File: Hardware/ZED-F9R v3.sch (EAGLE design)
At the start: 75 parts, among them J3 QWIIC_RIGHT_ANGLE, J4 QWIIC_RIGHT_ANGLE, U1 DUAL-OPTO_HCPL-073LSOIC-8, U2 U-BLOX_ZED_F9R, U3 UHS_INVERTER_SCHMITT_TRIGGERS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, U4 UHS_INVERTER_SCHMITT_TRIGGERS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, U5 3.3V

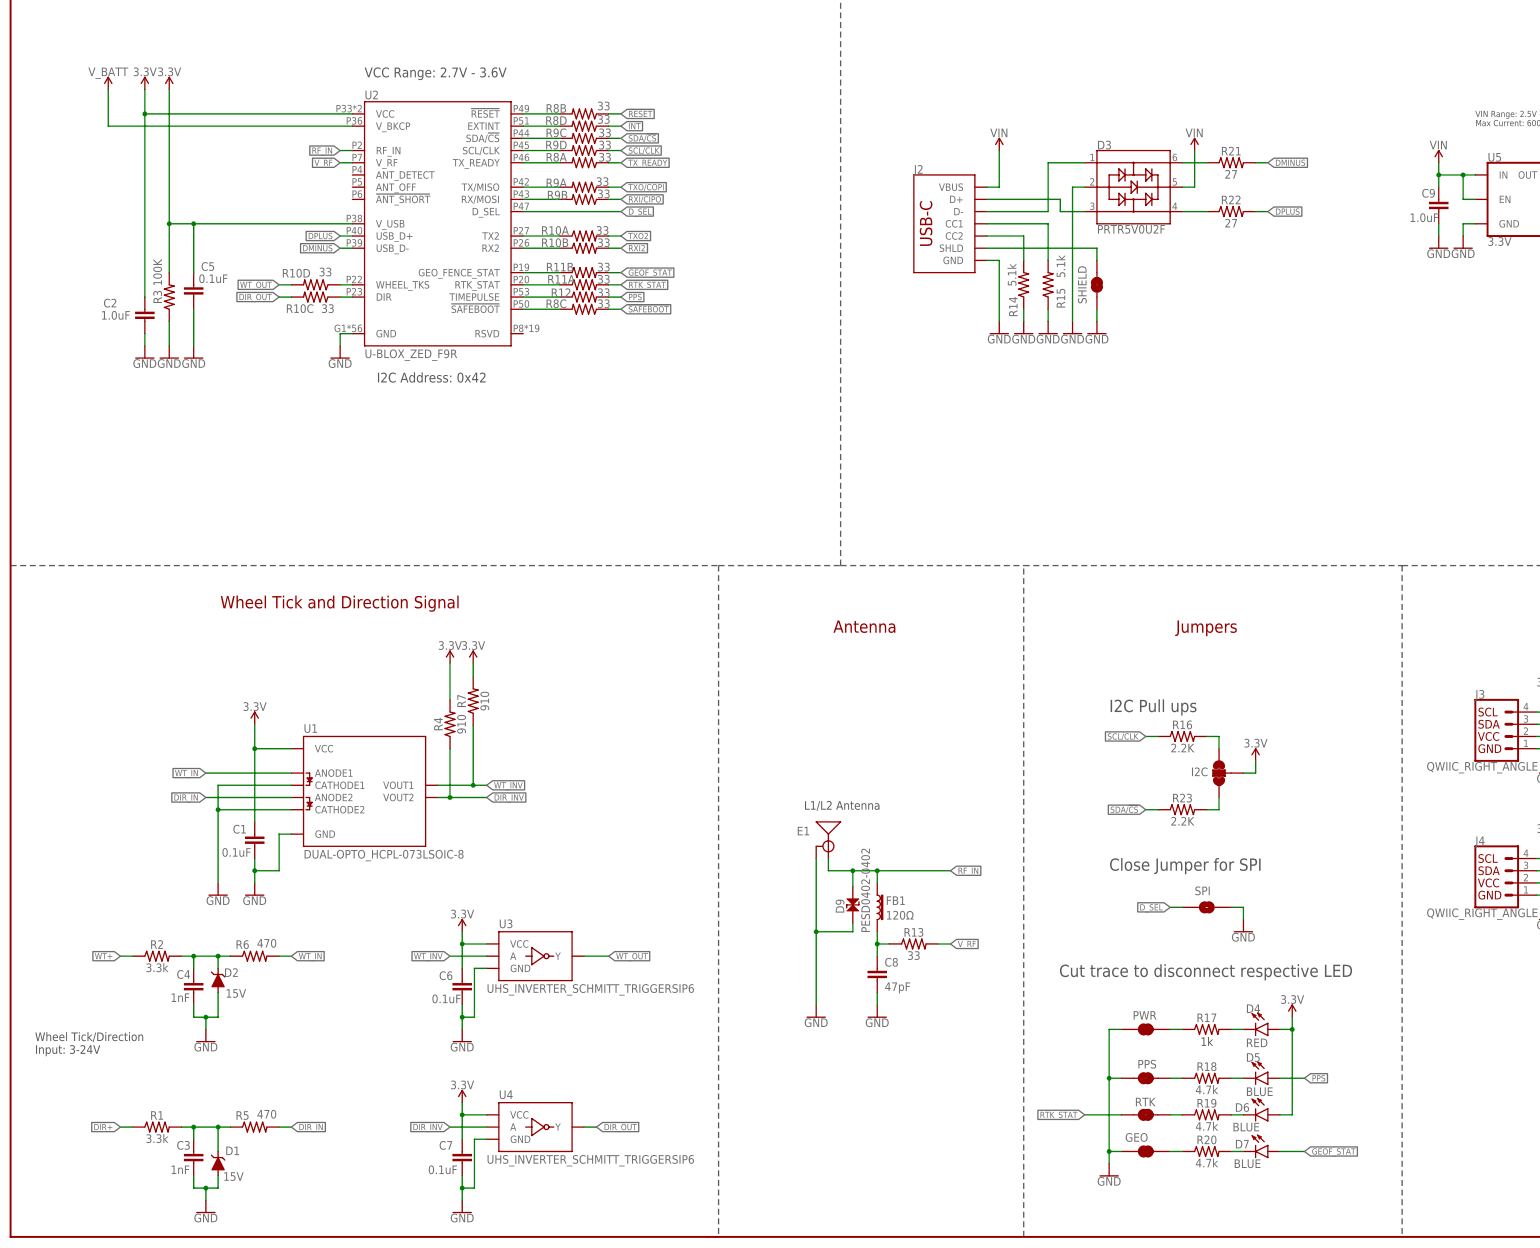
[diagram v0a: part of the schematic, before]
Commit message: Adds more capacitance to power lines
* Fixes various trace irregularities
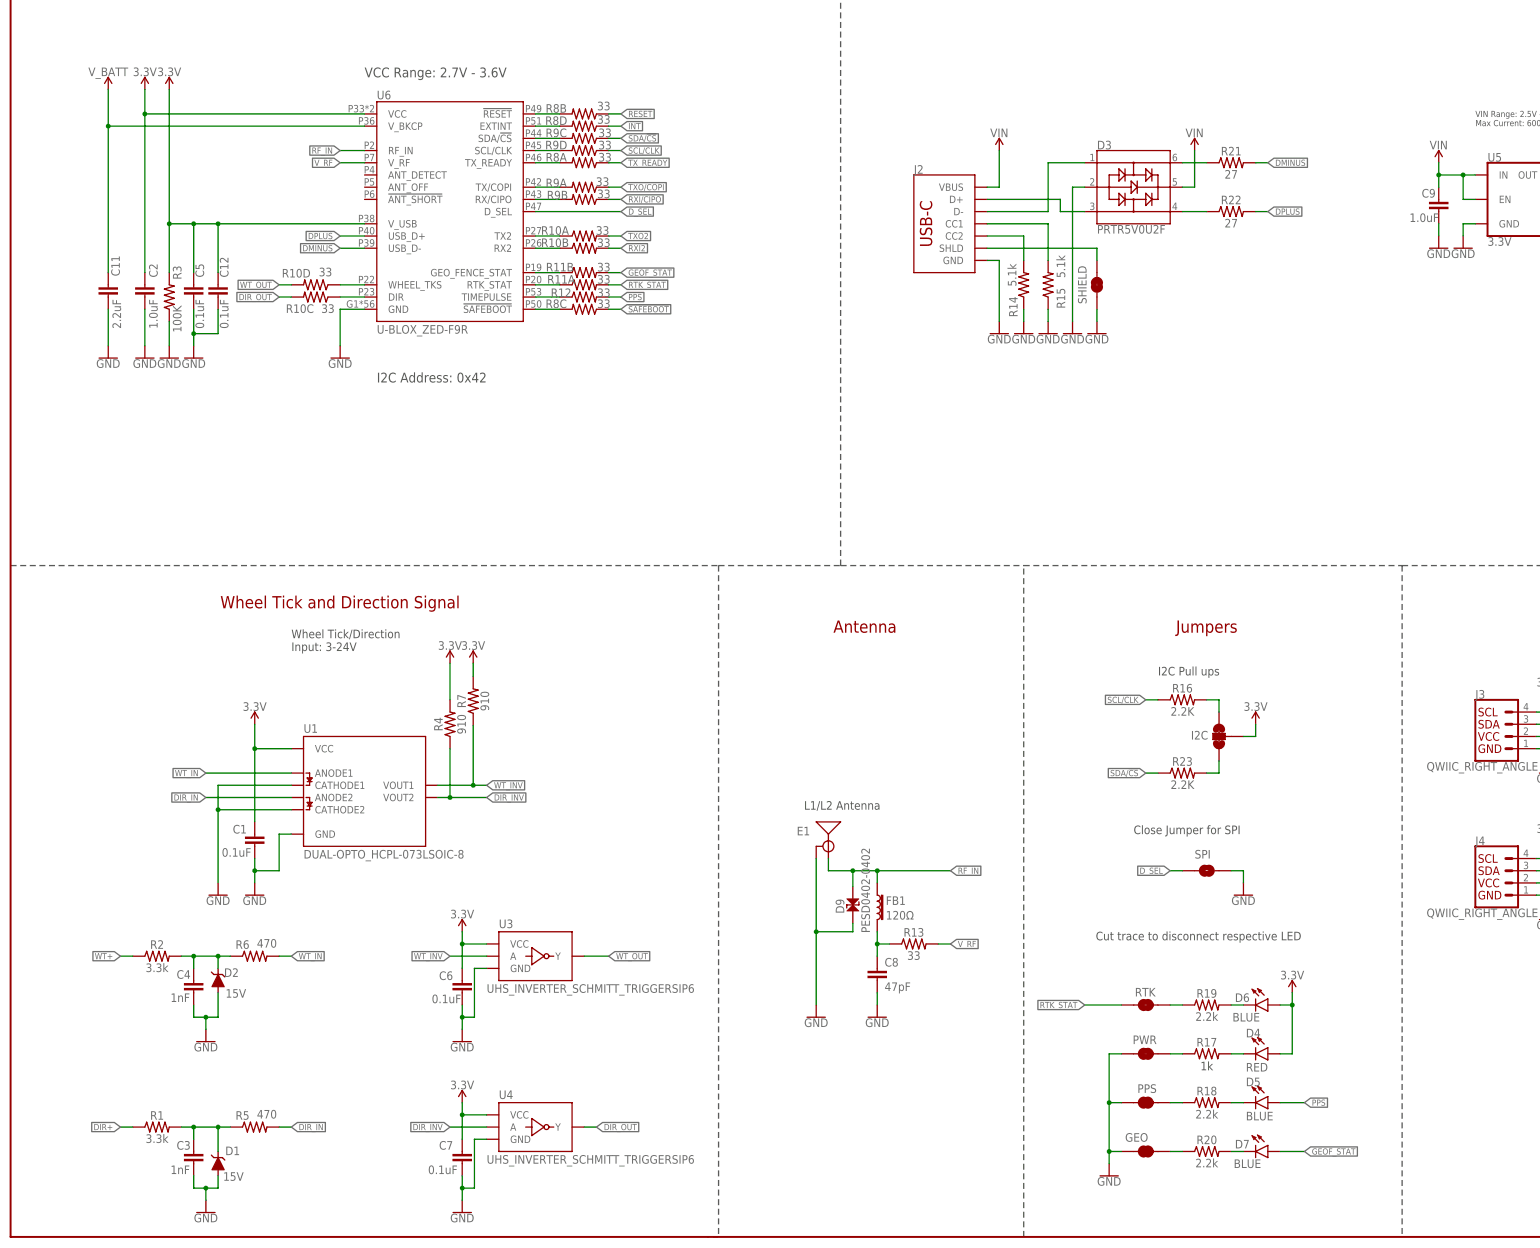
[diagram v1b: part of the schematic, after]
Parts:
- removed U2: U-BLOX_ZED_F9R, SparkFun-GPS:U-BLOX_ZED_F9R
- added C11: 2.2uF, SparkFun-Capacitors:2.2UF-0402_TIGHT-10V-10%-X5R
- added C12: 0.1uF, SparkFun-Capacitors:0.1UF-0402T-6.3V-10%-X7R
- added U6: U-BLOX_ZED-F9R, SparkFun-GPS:U-BLOX_ZED-F9R
- R18, R19, R20: value 4.7k -> 2.2k; device SparkFun-Resistors:4.7KOHM-0603-1/10W-1% -> SparkFun-Resistors:2.2KOHM-0603-1/10W-1%
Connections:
- net 3.3V: now also C12.1, U6.VCC, U6.V_USB; no longer U2.VCC, U2.V_USB
- net DMINUS: now also U6.USB_D-; no longer U2.USB_D-
- net DPLUS: now also U6.USB_D+; no longer U2.USB_D+
- net D_SEL: now also U6.D_SEL; no longer U2.D_SEL
- net GND: now also C11.2, C12.2, U6.GND; no longer U2.GND
- net N$11: now also U6.!RESET!; no longer U2.!RESET!
- net N$12: now also U6.EXTINT; no longer U2.EXTINT
- net N$16: now also U6.SDA/!CS!; no longer U2.SDA/!CS!
- net N$17: now also U6.SCL/CLK; no longer U2.SCL/CLK
- net N$18: now also U6.TX_READY; no longer U2.TX_READY
- net N$19: now also U6.TX/COPI; no longer U2.TX/MISO
- net N$20: now also U6.RX/CIPO; no longer U2.RX/MOSI
- net N$21: now also U6.TX2; no longer U2.TX2
- net N$26: now also U6.RX2; no longer U2.RX2
- net N$27: now also U6.GEO_FENCE_STAT; no longer U2.GEO_FENCE_STAT
- net N$28: now also U6.RTK_STAT; no longer U2.RTK_STAT
- net N$29: now also U6.TIMEPULSE; no longer U2.TIMEPULSE
- net N$30: now also U6.!SAFEBOOT!; no longer U2.!SAFEBOOT!
- net N$31: now also U6.WHEEL_TKS; no longer U2.WHEEL_TKS
- net N$32: now also U6.DIR; no longer U2.DIR
- net RF_IN: now also U6.RF_IN; no longer U2.RF_IN
- net V_BATT: now also C11.1, U6.V_BKCP; no longer U2.V_BKCP
- net V_RF: now also U6.V_RF; no longer U2.V_RF
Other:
- moved on the sheet: C2, D4, D5, D6, I2C, PPS, PWR, R16, R17, R18, R19, R23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
